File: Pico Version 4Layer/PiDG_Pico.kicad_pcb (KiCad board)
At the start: 4 copper layers, 126 x 126 mm, 48 parts, among them J1 Conn_02x05_Odd_Even, J10 Trig, J11 Laser Enable, J12 Pixel Reset, J14 Pico Socket A, J15 Pico Socket B, J16 Laser En/PWM Trig/GND, J2 Conn_02x05_Odd_Even, J3 Conn_02x05_Odd_Even, J4 Conn_02x05_Odd_Even, J5 Conn_02x05_Odd_Even, J6 Conn_02x05_Odd_Even, J7 Laser 1, J8 Laser 2, U1 74LVC1G04, U10 74LVC1G08, U12 74LVC1G08, U13 UCC27524, U2 SN74LVC04AD, U3 74LVC1G04, U4 SN74LVC04AD, U5 74LVC1G04, U6 SN74LVC04AD, U7 74LVC1G08, U8 74LVC1G08

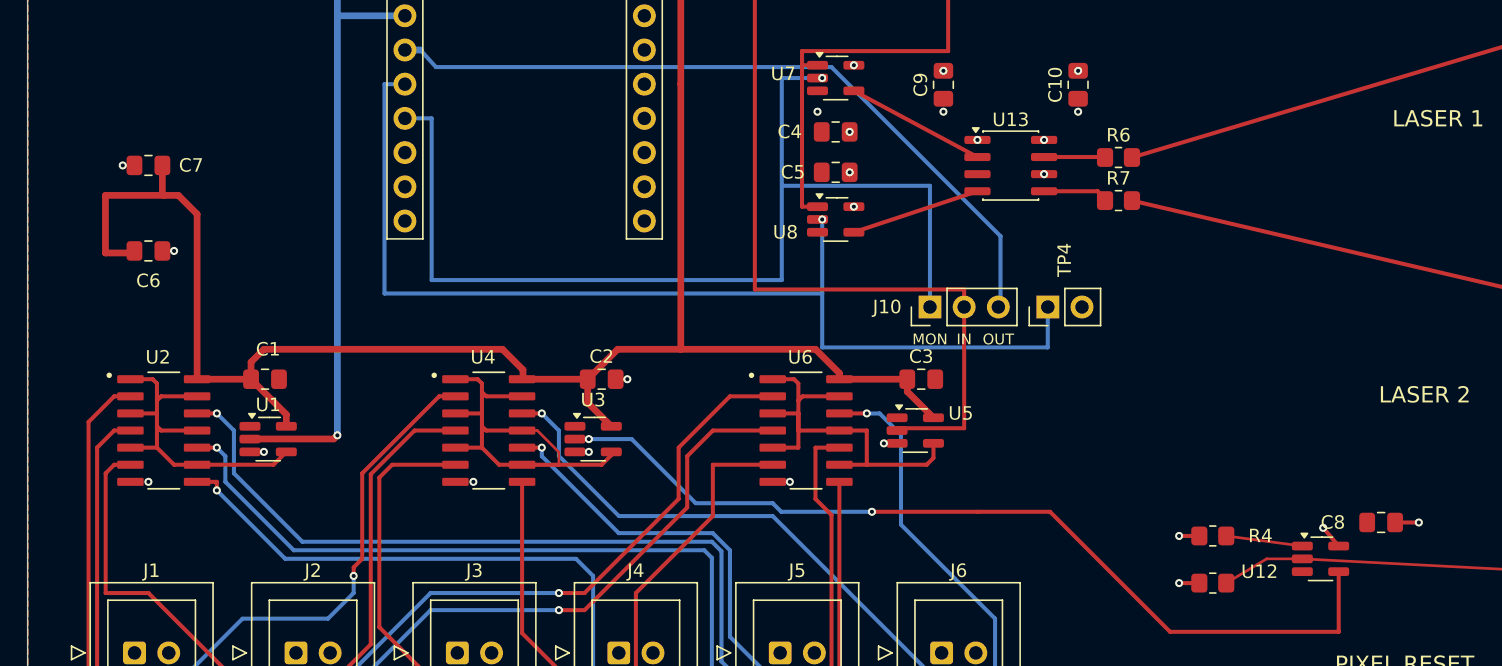
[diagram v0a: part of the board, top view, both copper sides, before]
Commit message: Restore 1.8 V camera I/O rail; rebuild pixel-reset input as a 3.3 V Schmitt
The IDS UE-39B0XCP-E datasheet (part 1011378, rev 2026-01-09) documents
its I/O connector pins 3/4/5 -- TDRSTN, Trigger input, SYNC -- as
"(sensor), 1.8 V". The Teensy design's 1.8 V rail was therefore the
camera signalling rail, not vestigial. The Pico redesign had deleted it
and run the camera bank at 3.3 V, which would have driven 3.3 V into
1.8 V sensor pins on all 18 lines of six cameras. The harness does no
level translation, so the board itself must present 1.8 V.

Camera rail:
- Restore U9 = NCP718xSN180 (fixed 1.8 V LDO) at the Teensy's exact
  site. Feed it from +5 V rather than +3V3: NCP718 accepts 2.5-24 V, and
  +5 V is the In2 plane, reachable with one via.
- U1-U6 back on +1V8 via the five original camera-bank rail symbols.
  No part changes: SN74LVC04A / 74LVC1G04 inputs are 5.5 V tolerant
  independent of VCC, so at 1.8 V the bank itself translates down from
  the Pico's 3.3 V. At 1.8 V the drivers' 60-113 ohm output impedance
  also series-matches the ribbon, so no series resistors are needed.
- C6 -> 1 uF input cap, C7 -> 2.2 uF output cap. The Teensy's 1.8 V rail
  had only 4 x 0.1 uF, below NCP718's documented >= 1 uF stability floor.
- Board: the redesign had deleted U9 and bridged its OUT pad straight to
  the IN side with one segment, merging the two rails. Deleting that
  bridge and re-netting restores the Teensy's original +1V8 output route
  unchanged. U9's GND pad gets a via under the body to the In1 plane.

Pixel-reset input:
- U12 74LVC1G08 @ +5 V -> 74LVC1G17 Schmitt buffer @ +3V3 (drop-in on
  the SOT-23-5 pads). At VCC = 5 V an LVC input needs 0.7 x VCC = 3.5 V
  to read high, so a 3.3 V source could not reliably release reset, and
  a bare BNC input had no hysteresis. At 3.3 V the 1G17 switches low
  below 0.89 V and high above ~1.92-2.1 V with 0.5-0.8 V hysteresis, and
  tolerates 5.5 V input: 3.3 V / 5 V CMOS, TTL and open-drain sources
  all work. A 1.8 V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
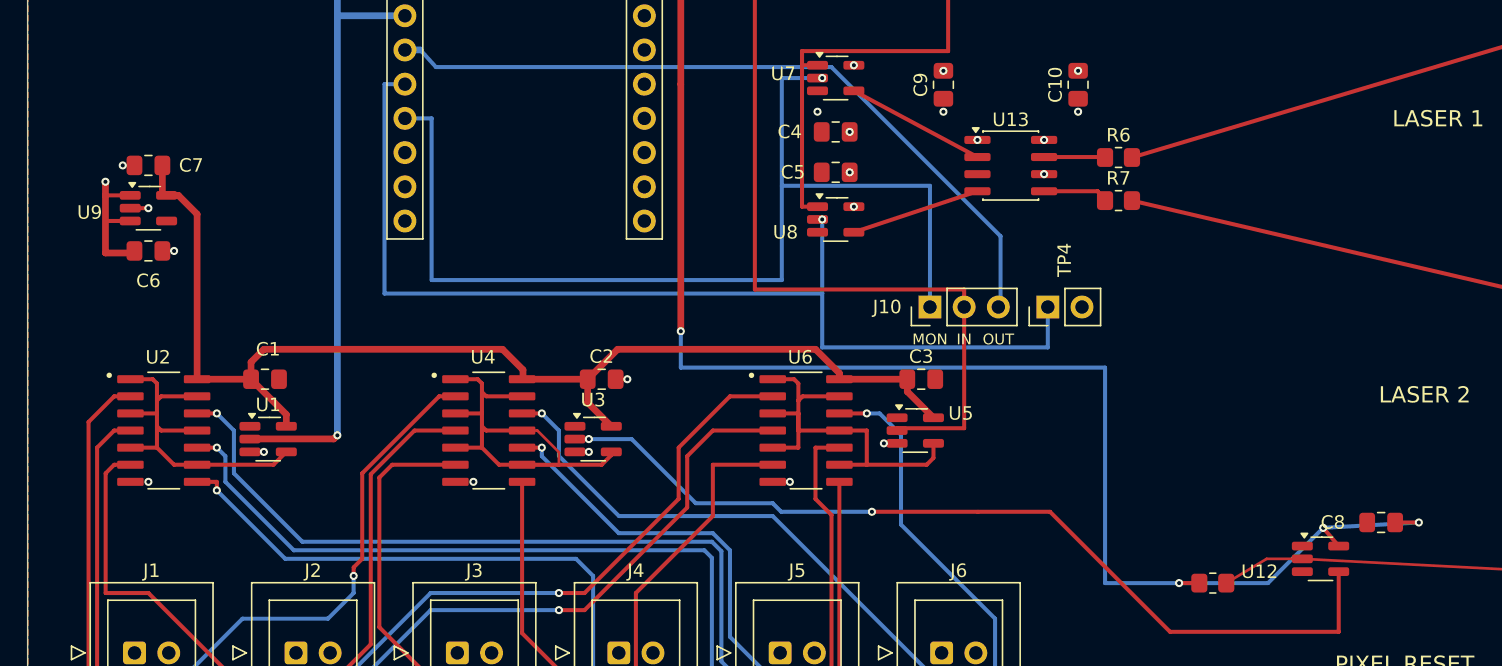
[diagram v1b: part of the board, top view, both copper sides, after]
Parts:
- removed R4: 3k3, Resistor_SMD:R_0805_2012Metric_Pad1.20x1.40mm_HandSolder
- added U9: NCP718xSN180, Package_TO_SOT_SMD:SOT-23-5_HandSoldering, F.Cu at (141.0, 93.7)
- C6: value 0.1uF -> 1uF
- C7: value 0.1uF -> 2.2uF
- U12: value 74LVC1G08 -> 74LVC1G17
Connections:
- C1 pad 1: +3V3 -> +1V8
- C2 pad 1: +3V3 -> +1V8
- C3 pad 1: +3V3 -> +1V8
- C6 pad 1: +3V3 -> +5V
- C7 pad 1: +3V3 -> +1V8
- C8 pad 1: +5V -> +3V3
- R5 pad 1: +5V -> +3V3
- U1 pad 5: +3V3 -> +1V8
- U12 pad 1: PIXRST_GATE_EN -> unconnected-(U12-NC-Pad1)
- U12 pad 5: +5V -> +3V3
- U2 pad 14: +3V3 -> +1V8
- U3 pad 5: +3V3 -> +1V8
- U4 pad 14: +3V3 -> +1V8
- U5 pad 5: +3V3 -> +1V8
- U6 pad 14: +3V3 -> +1V8
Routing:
- net +1V8: track 0.00 -> 88.0 mm
- net +3V3: track 149.1 -> 129.2 mm, vias 0 -> 4
- net PIXRST_GATE_EN: track 5.70 -> 0.00 mm
- net +5V: track 6.54 -> 11.2 mm, vias 16 -> 13
- net GND: track 2.93 -> 4.28 mm, vias 12 -> 13

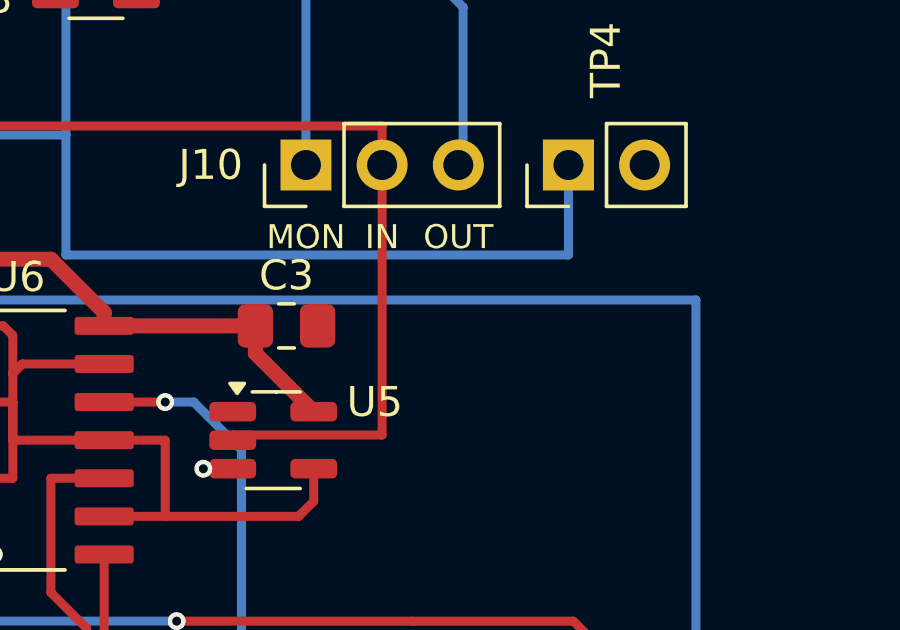
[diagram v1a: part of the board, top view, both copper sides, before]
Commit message: Add R9 pull-down on the J10 camera-trigger select node
With no shunt fitted on J10, PWM_TRIG_TAP (J10.2, J16.2, U5.2) had no
defined level: U5's input floated on ~145 mm of trace, which also runs
up across the board to J16.2, and all six camera trigger lines followed
it.

R9 (10k, 0805) now pulls it to GND, so with J10 unshunted the triggers
idle low -- their inactive state. 10k rather than a weaker pull: U5 runs
from the 1.8 V rail (VIL 0.63 V), and at the datasheet's worst-case 5 uA
input leakage 100k would sit at 0.5 V with only 0.13 V to spare, where
10k holds it at 0.05 V and rejects coupled noise ten times better. The
selected GPIO sees an extra 330 uA when J10 is shunted. Same value as R8,
so no new BOM line.

Placed at (203.5, 106) rot 90 beside U5's input run with a 2 mm link;
worst-case clearance 1.09 mm. B.Cu copper runs directly underneath, so
its ground pad connects through the F.Cu pour rather than a via --
confirmed by the kicad-cli unconnected-items check.

Hardware.md: J10 open item removed; the laser-impedance item reworded to
make clear J7/J8 are outputs and the impedance in question is the
laser's own trigger input at the far end of the cable.

ERC 0, DRC 0, 0 unconnected items, board vs schematic nets exact.

Co-Authored-By: Claude Opus 5.5 (1M context) <noreply@anthropic.com>
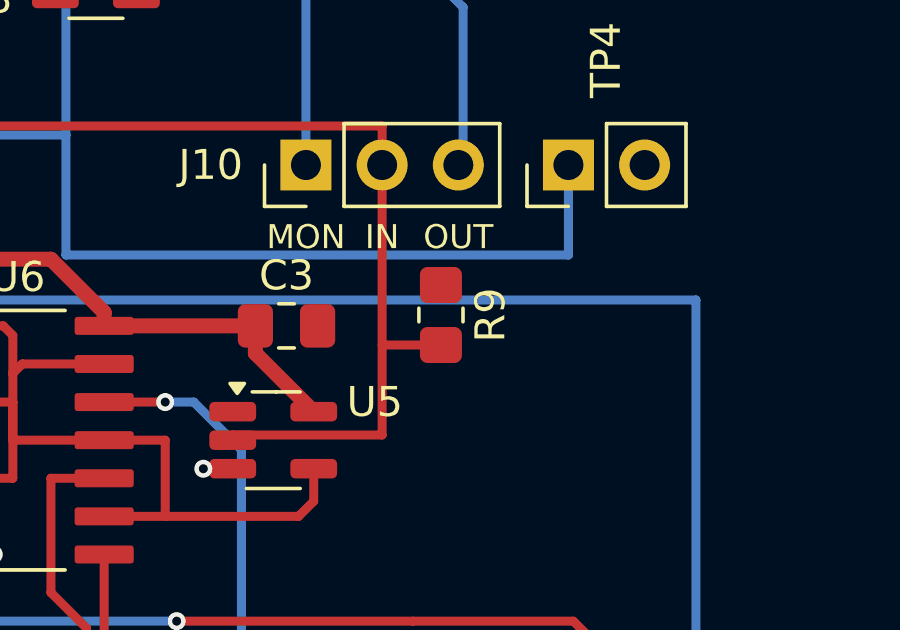
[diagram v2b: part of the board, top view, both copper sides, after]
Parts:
- added R9: 10k, Resistor_SMD:R_0805_2012Metric_Pad1.20x1.40mm_HandSolder, F.Cu at (203.5, 106.0)
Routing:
- net PWM_TRIG_TAP: track 150.2 -> 152.2 mm
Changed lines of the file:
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@@
 		)
 	)
+	(footprint "Resistor_SMD:R_0805_2012Metric_Pad1.20x1.40mm_HandSolder"
+		(layer "F.Cu")
+		(at 203.5 106 90)
+		(descr "Resistor SMD 0805 (2012 Metric), square (rectangular) end terminal, IPC-7351 nominal with elongated pad for handsoldering. (Body size source: IPC-SM-782 page 72, https://www.pcb-3d.com/wordpress/wp-content/uploads/ipc-sm-782a_amendment_1_and_2.pdf)")
+		(tags "resistor handsolder")
+		(property "Reference" "R9"
+			(at 0 1.65 90)
+			(layer "F.SilkS")
+			(effects
+				(font
+					(size 1 1)
+					(thickness 0.15)
+				)
+			)
+		)
+		(property "Value" "10k"
+			(at 0.127 -1.778 90)
+			(layer "F.Fab")
+			(effects
+				(font
+					(size 1 1)
+					(thickness 0.15)
+				)
+			)
+		)
+		(property "Datasheet" "~"
+			(at 0 0 90)
+			(layer "F.Fab")
+			(hide yes)
+			(effects
+				(font
+					(size 1.27 1.27)
+					(thickness 0.15)
+				)
+			)
+		)
+		(property "Description" "Pull-down on PWM_TRIG_TAP: defines U5 input when J10 has no shunt"
+			(at 0 0 90)
+			(layer "F.Fab")
+			(hide yes)
+			(effects
+				(font
+					(size 1.27 1.27)
+					(thickness 0.15)
+				)
+			)
+		)
+		(property ki_fp_filters "R_*")
+		(attr smd)
+		(duplicate_pad_numbers_are_jumpers no)
+		(fp_line
+			(start -0.227064 -0.735)
+			(end 0.227064 -0.735)
+			(stroke
+				(width 0.12)
+				(type solid)
+			)
+			(layer "F.SilkS")
+		)
+		(fp_line
+			(start -0.227064 0.735)
+			(end 0.227064 0.735)
+			(stroke
+				(width 0.12)
+				(type solid)
+			)
+			(layer "F.SilkS")
+		)
+		(fp_rect
+			(start -1.85 -0.95)
+			(end 1.85 0.95)
+			(stroke
+				(width 0.05)
+				(type solid)
+			)
+			(fill no)
+			(layer "F.CrtYd")
+		)
+		(fp_rect
+			(start -1 -0.625)
+			(end 1 0.625)
+			(stroke
+				(width 0.1)
+				(type solid)
+			)
+			(fill no)
+			(layer "F.Fab")
+		)
+		(fp_text user "${REFERENCE}"
+			(at 0 0 0)
+			(layer "F.Fab")
+			(effects
+				(font
+					(size 0.5 0.5)
+					(thickness 0.08)
+				)
+			)
+		)
+		(pad "1" smd roundrect
+			(at -1 0 90)
+			(size 1.2 1.4)
+			(layers "F.Cu" "F.Mask" "F.Paste")
+			(roundrect_rratio 0.208333)
+			(net "PWM_TRIG_TAP")
+			(pintype "passive")
+		)
+		(pad "2" smd roundrect
+			(at 1 0 90)
+			(size 1.2 1.4)
+			(layers "F.Cu" "F.Mask" "F.Paste")
+			(roundrect_rratio 0.208333)
+			(net "GND")
+			(pintype "passive")
+		)
+		(embedded_fonts no)
+		(model "${KICAD10_3DMODEL_DIR}/Resistor_SMD.3dshapes/R_0805_2012Metric.step"
+			(offset
+				(xyz 0 0 0)
+			)
+			(scale
+				(xyz 1 1 1)
+			)
+			(rotate
+				(xyz 0 0 0)
+			)
+		)
+	)
 	(footprint "Connector_Coaxial:BNC_Amphenol_B6252HB-NPP3G-50_Horizontal"
 		(layer "F.Cu")
@@
 		(width 0.3)
 		(layer "F.Cu")
+		(net "PWM_TRIG_TAP")
+	)
+	(segment
+		(start 203.5 107)
+		(end 201.54 107)
+		(width 0.3)
+		(layer "F.Cu")

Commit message: Laser path: AHCT gates, firmware safety limits for PicoLas LDP-V drivers
The laser outputs must trigger PicoLas LDP-V 10-70 and LDP-V 240-100
drivers. This commit fixes the two problems in that path that need no
design decision. The third -- output amplitude -- is documented as the
blocking open item pending a choice of supply for a 10 V driver rail.

U7, U8, U10: 74LVC1G08 -> 74AHCT1G08
- At VCC = 5 V an LVC input needs 0.7 x VCC = 3.5 V to read high, but
  U7/U8 take their pulses straight from 3.3 V Pico GPIOs -- outside the
  guaranteed operating range at every normal USB voltage. AHCT has TTL
  input thresholds (high above 2.0 V): ~1.3 V of margin.
- U10 swapped too: the J11/R2/R8 arming divider now clears VIH by 1.76 V
  instead of ~260 mV, and an external interlock on J16.1 can be 3.3 V.
- 74AHCT1G08 extends 74LVC1G08 in the KiCad library: same body, same
  pins, same SOT-23-5 footprint. No wiring or layout change.

Firmware laser safety limits
- LDP-V 10-70: 10 ns - 1 us pulse, max duty factor 0.1 %.
  LDP-V 240-100: 60 ns - >1 us, 7.5 %. CH1/CH2 share one width, so the
  10-70 governs.
- The previous default -- 2 us at 1 kHz -- was twice the 10-70's maximum
  pulse width and twice its duty limit, applied at power-up before any
  command was sent.
- Default WIDTH is now 100 ns, inside both drivers' ranges.
- applyPulseParams() rejects WIDTH > 1000 ns or WIDTH x FREQ > 0.1 %
  (kLaserMaxWidthNs, kLaserMaxDutyPpm). HELP text states the limits.

Documented, not yet fixed: the LDP-V trigger inputs are 50 ohm
terminated and need 4.5-5.2 V high / <= 0.2 V low. Today's 5 V rail
through 47 ohm delivers 2.1-2.6 V; 0 ohm series still spans 3.8-5.0 V.
A regulated 10 V rail with R6/R7 = 48.7 ohm gives 4.55-5.11 V across all
tolerances.

ERC 0, DRC 0, 0 unconnected. Firmware builds.

Co-Authored-By: Claude Opus 5.5 (1M context) <noreply@anthropic.com>
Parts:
- U10, U7, U8: value 74LVC1G08 -> 74AHCT1G08
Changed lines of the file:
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@@
 			)
 		)
-		(property "Value" "74LVC1G08"
+		(property "Value" "74AHCT1G08"
 			(at 0 2.9 0)
 			(layer "F.Fab")
@@
 			)
 		)
-		(property "Datasheet" "https://www.ti.com/lit/ds/symlink/sn74lvc1g08.pdf"
+		(property "Datasheet" "http://www.ti.com/lit/sg/scyt129e/scyt129e.pdf"
 			(at 0 0 0)
 			(unlocked yes)
@@
 			)
 		)
-		(property "Value" "74LVC1G08"
+		(property "Value" "74AHCT1G08"
 			(at 0 2.9 0)
 			(layer "F.Fab")
@@
 			)
 		)
-		(property "Datasheet" "https://www.ti.com/lit/ds/symlink/sn74lvc1g08.pdf"
+		(property "Datasheet" "http://www.ti.com/lit/sg/scyt129e/scyt129e.pdf"
 			(at 0 0 0)
 			(unlocked yes)
@@
 			)
 		)
-		(property "Value" "74LVC1G08"
+		(property "Value" "74AHCT1G08"
 			(at 0 2.9 0)
 			(layer "F.Fab")
@@
 			)
 		)
-		(property "Datasheet" "https://www.ti.com/lit/ds/symlink/sn74lvc1g08.pdf"
+		(property "Datasheet" "http://www.ti.com/lit/sg/scyt129e/scyt129e.pdf"
 			(at 0 0 0)
 			(unlocked yes)
